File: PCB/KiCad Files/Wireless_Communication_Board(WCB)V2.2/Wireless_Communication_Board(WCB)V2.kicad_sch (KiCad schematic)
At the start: 36 parts, among them J1 USB_B_Micro, J2 Power In, J3 Conn_01x04, J4 Conn_01x04, J5 Conn_01x04, J6 Conn_01x04, J7 Conn_01x04, Q2 UMH3N, U1 ESP32-PICO-MINI-02, U2 CP2102N-A02-GQFN28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

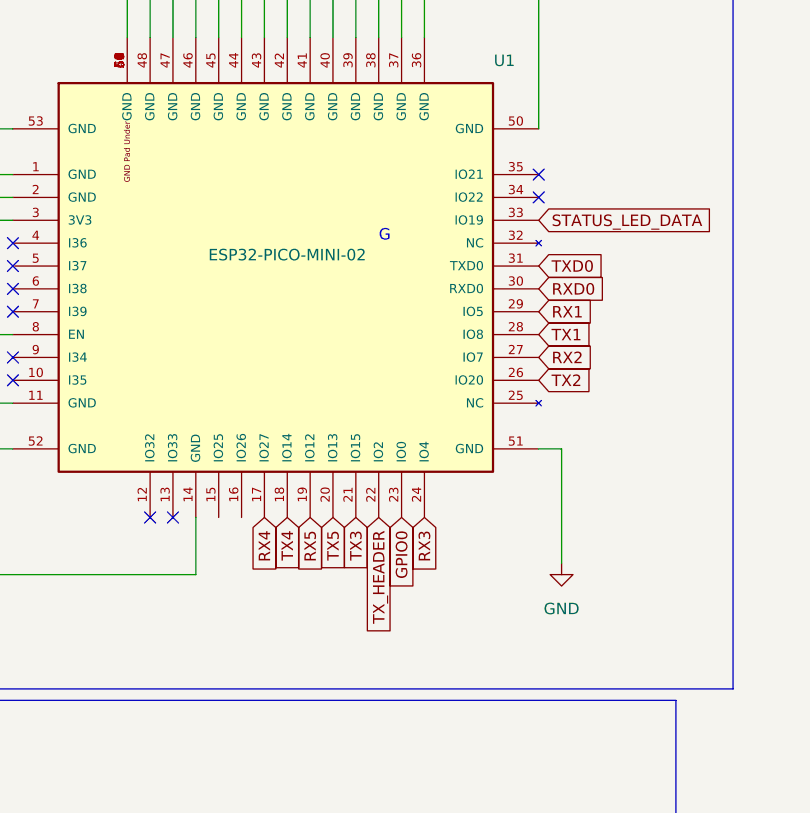
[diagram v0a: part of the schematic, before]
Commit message: Added WCB V2.2 and working on the code some.
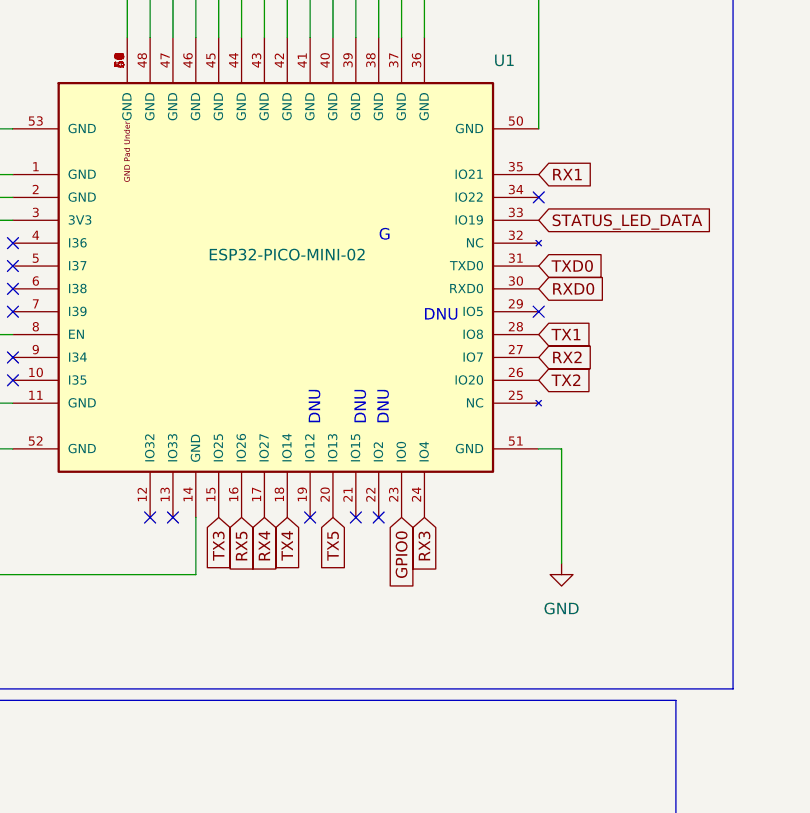
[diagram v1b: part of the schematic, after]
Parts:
- R16: LCSC C852799 -> C114949
- R5: LCSC C270604 -> C319605
- S1: Manufacturers Part Number TL3342F160QG -> TS-1076S-A6B3
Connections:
- net RX1: now also U1.35 (IO21); no longer U1.29 (IO5)
- net RX5: now also U1.16 (IO26); no longer U1.19 (IO12)
- net TX3: now also U1.15 (IO25); no longer U1.21 (IO15)
- net TX_HEADER: no longer names the net of U1.22 (IO2)
- no-connect marks 30 -> 33
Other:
- note added: "DNU"
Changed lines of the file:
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@@
   (junction (at 96.52 20.32) (diameter 0) (color 0 0 0 0)
   )
+  (no_connect (at 93.98 78.74))
   (no_connect (at 259.08 27.94))
   (no_connect (at 152.4 168.91))
@@
   (no_connect (at 71.12 78.74))
   (no_connect (at 55.88 63.5))
-  (no_connect (at 114.3 40.64))
+  (no_connect (at 114.3 55.88))
   (no_connect (at 73.66 78.74))
   (no_connect (at 114.3 43.18))
+  (no_connect (at 96.52 78.74))
   (no_connect (at 248.92 27.94))
   (no_connect (at 233.68 38.1))
@@
   (no_connect (at 259.08 66.04))
   (no_connect (at 184.15 43.18))
+  (no_connect (at 88.9 78.74))
   (polyline (pts (xy 135.89 15.24) (xy 135.89 97.79))
     (stroke (width 0) (type default) (color 0 0 0 0))
@@
     (effects (font (size 1.27 1.27)) (justify left bottom))
   )
+  (text "DNU" (at 90.17 68.58 90)
+    (effects (font (size 1.27 1.27)) (justify left bottom))
+  )
   (text "G" (at 41.8215 51.8785 0)
     (effects (font (size 1.27 1.27)) (justify left bottom))
@@
     (effects (font (size 1.27 1.27)) (justify left bottom))
   )
+  (text "DNU" (at 97.79 68.58 90)
+    (effects (font (size 1.27 1.27)) (justify left bottom))
+  )
   (text "G" (at 36.83 52.07 0)
     (effects (font (size 1.27 1.27)) (justify left bottom))
@@
     (effects (font (size 1.27 1.27)) (justify left bottom))
   )
+  (text "DNU" (at 95.25 68.58 90)
+    (effects (font (size 1.27 1.27)) (justify left bottom))
+  )
   (text "Status LEDs" (at 104.14 144.78 0)
     (effects (font (size 1.27 1.27)) (justify left bottom))
@@
   (text "0 left" (at 222.25 106.68 0)
     (effects (font (size 1.27 1.27)) (justify left bottom))
+  )
+  (text "DNU" (at 105.41 57.15 180)
+    (effects (font (size 1.27 1.27)) (justify right bottom))
   )
   (text "G" (at 260.35 101.6 0)
@@
     )
   )
-  (global_label "TX3" (shape input) (at 93.98 78.74 270) (fields_autoplaced)
-    (effects (font (size 1.27 1.27)) (justify right))
-    (property "Intersheet References" "${INTERSHEET_REFS}" (id 0) (at 94.0594 84.5398 90)
+  (global_label "TX3" (shape input) (at 78.74 78.74 270) (fields_autoplaced)
+    (effects (font (size 1.27 1.27)) (justify right))
+    (property "Intersheet References" "${INTERSHEET_REFS}" (id 0) (at 78.8194 84.5398 90)
       (effects (font (size 1.27 1.27)) (justify right) hide)
     )
@@
     )
   )
-  (global_label "TX_HEADER" (shape input) (at 96.52 78.74 270) (fields_autoplaced)
-    (effects (font (size 1.27 1.27)) (justify right))
-    (property "Intersheet References" "${INTERSHEET_REFS}" (id 0) (at 96.4406 91.555 90)
-      (effects (font (size 1.27 1.27)) (justify right) hide)
-    )
-  )
-  (global_label "RX1" (shape input) (at 114.3 55.88 0) (fields_autoplaced)
+  (global_label "RX1" (shape input) (at 114.3 40.64 0) (fields_autoplaced)
     (effects (font (size 1.27 1.27)) (justify left))
-    (property "Intersheet References" "${INTERSHEET_REFS}" (id 0) (at 120.4021 55.8006 0)
+    (property "Intersheet References" "${INTERSHEET_REFS}" (id 0) (at 120.4021 40.5606 0)
       (effects (font (size 1.27 1.27)) (justify left) hide)
     )
@@
     )
   )
-  (global_label "RX5" (shape input) (at 88.9 78.74 270) (fields_autoplaced)
-    (effects (font (size 1.27 1.27)) (justify right))
-    (property "Intersheet References" "${INTERSHEET_REFS}" (id 0) (at 88.8206 84.8421 90)
+  (global_label "RX5" (shape input) (at 81.28 78.74 270) (fields_autoplaced)
+    (effects (font (size 1.27 1.27)) (justify right))
+    (property "Intersheet References" "${INTERSHEET_REFS}" (id 0) (at 81.2006 84.8421 90)
       (effects (font (size 1.27 1.27)) (justify right) hide)
     )
@@
       (effects (font (size 1.27 1.27)) hide)
     )
-    (property "LCSC" "C852799" (id 8) (at 129.54 168.91 0)
+    (property "LCSC" "C114949" (id 8) (at 129.54 168.91 0)
       (effects (font (size 1.27 1.27)) hide)
     )
@@
       (effects (font (size 1.27 1.27)) hide)
     )
-    (property "LCSC" "C270604" (id 8) (at 232.41 74.93 0)
+    (property "LCSC" "C319605" (id 8) (at 232.41 74.93 0)
       (effects (font (size 1.27 1.27)) hide)
     )
@@
       (effects (font (size 1.27 1.27)) hide)
     )
-    (property "Manufacturers Part Number" "TL3342F160QG" (id 6) (at 26.67 69.85 0)
-      (effects (font (size 1.27 1.27)) hide)
-    )
+    (property "Manufacturers Part Number" " TS-1076S-A6B3" (id 6) (at 26.67 69.85 0)
+      (effects (font (size 1.27 1.27)) hide)
+    )
